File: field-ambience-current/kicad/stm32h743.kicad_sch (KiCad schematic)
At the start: 45 parts, among them J4 SWD 1.27mm (SWCLK/GND/SWDIO), U1 STM32H743VIT6 (480MHz M7, LQF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, Y1 8MHz ABLS-8.000MHZ-B4-T (CL=1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

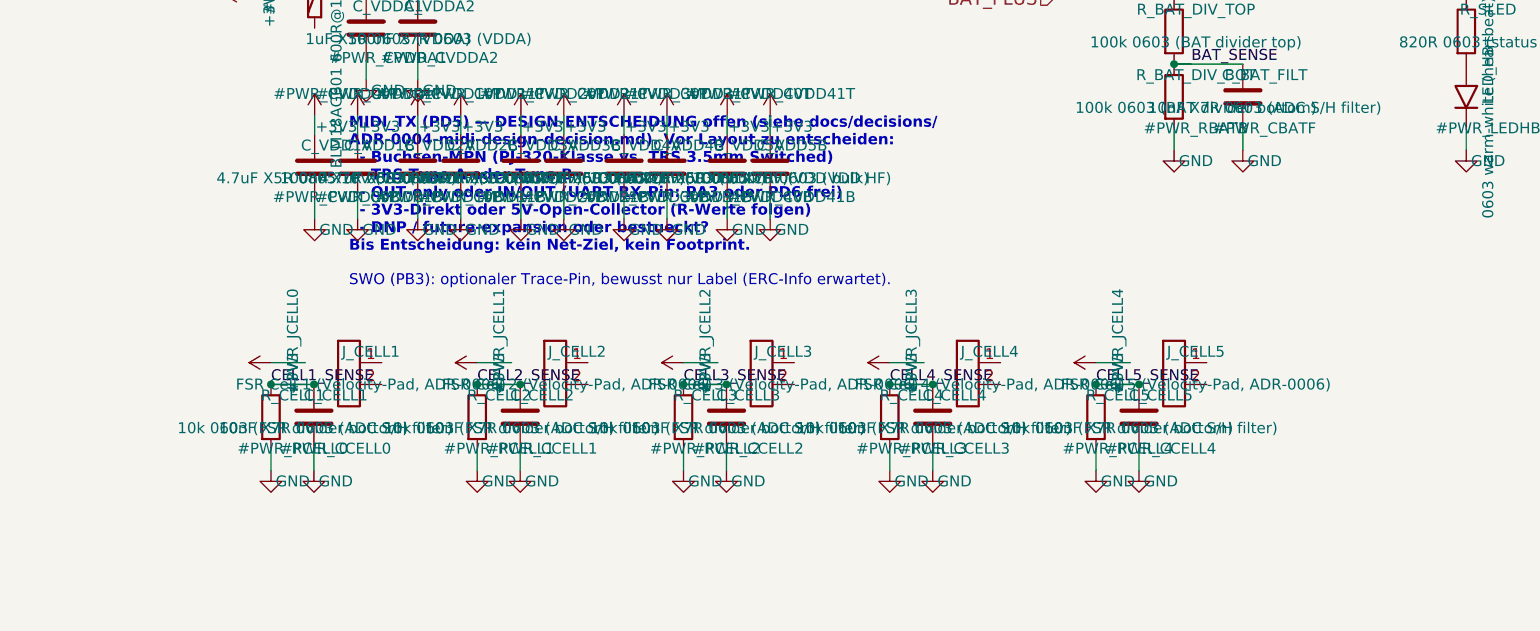
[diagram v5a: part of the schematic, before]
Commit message: pcb+fw(r18.14): Komponenten-Definition — 3D-Lib, 2 kritische BOM-Fixes, Encoder-Strategie (ADR-0012), Cell-Keys Magnetic-Hall (ADR-0013)
User-Direktive: Komponenten vor Layout definieren, 3D-Daten zu allem, Cells
wie HiChord mit langen Caps + Stabilizern, Encoder-Split + smooth + gleich
hoch + flach (Kick75), Encoder-UX-Bug fixen.

🔴 Kritische BOM-Fixes (via 3D-CAD-Abruf entdeckt):
- USB-C: C165935 war ein STF18N65M5-MOSFET (TO-220F-3)! Korrekt: C283540
  (TYPE-C-31-M-17, LCSC-verifiziert). Falsch seit r18.10.
- SW_BOOT: C720477 ist XUNPU TS-1088-AR02016 (nicht TS-1185A-C-A);
  FP von generisch TL3342 auf EasyEDA-verifiziertes SW_TS1088_SMD.

3D-STEP-Library:
- kicad/libraries/field_ambience.3dshapes/ — 9 Z-/Panel-kritische Modelle
- mechanical/3d_models/MANIFEST.md — Inventar, Höhen, Regenerier-Kommando

ADR-0012 Encoder-Strategie:
- EN3 (Display) einziger mit Push+Detents; EN1/2/4 = EC11E183440C smooth
  (ohne Rastung/Anschlag/Switch). Alle 4 = EC11E THT, gleiche Schaftlänge
  = gleich hoch, Ziel 20-22mm statt 24.5mm (EC11J-STEP-Beleg), Kick75-flach.
- EC11J SMD retired (NRND + zu hoch + Half-Step-Mismatch). FP-Verify: 0 offen.

Encoder-UX-Fix („zwei Klicks für 1%"):
- Bench-Encoder rastet jede halbe Quadratur-Periode → ENC_HALF_STEP Default=1
  (display_hw_test.c), Host-Test pinnt Full-Cycle-Modus explizit.
- encoders.c: per-Encoder substeps (Display 4, Smooth 2) + has_sw-Flag.
- 12/12 Test-Suiten PASS.

ADR-0013 Cell-Keys (ersetzt FSR aus ADR-0006):
- Gateron-LP-Magnetic-Switches (HiChord-Feel) + linearer Hall-Sensor pro
  Cell → Velocity = dPos/dt, Aftertouch firmware-offen. ADC-Pins unverändert.
- Lange Caps ≥2u mit LP-Stabilizern (Spacebar-Prinzip: Switch mittig,
  Support links/rechts).
- Schematic: J_CELL 1×2-FSR-Teiler → 1×3-Hall-Site + 1k-Serien-RC.
- Sensor-Kandidaten DRV5056A4/SS49E mit explizitem PINOUT-VERIFY (AP7361-Lektion).

Modifier-Buttons: SPEC stellt explizit klar — alle 5 identisch, momentary,
Latch-Zustand nur über LEDs (ADR-0008).

Scores: F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
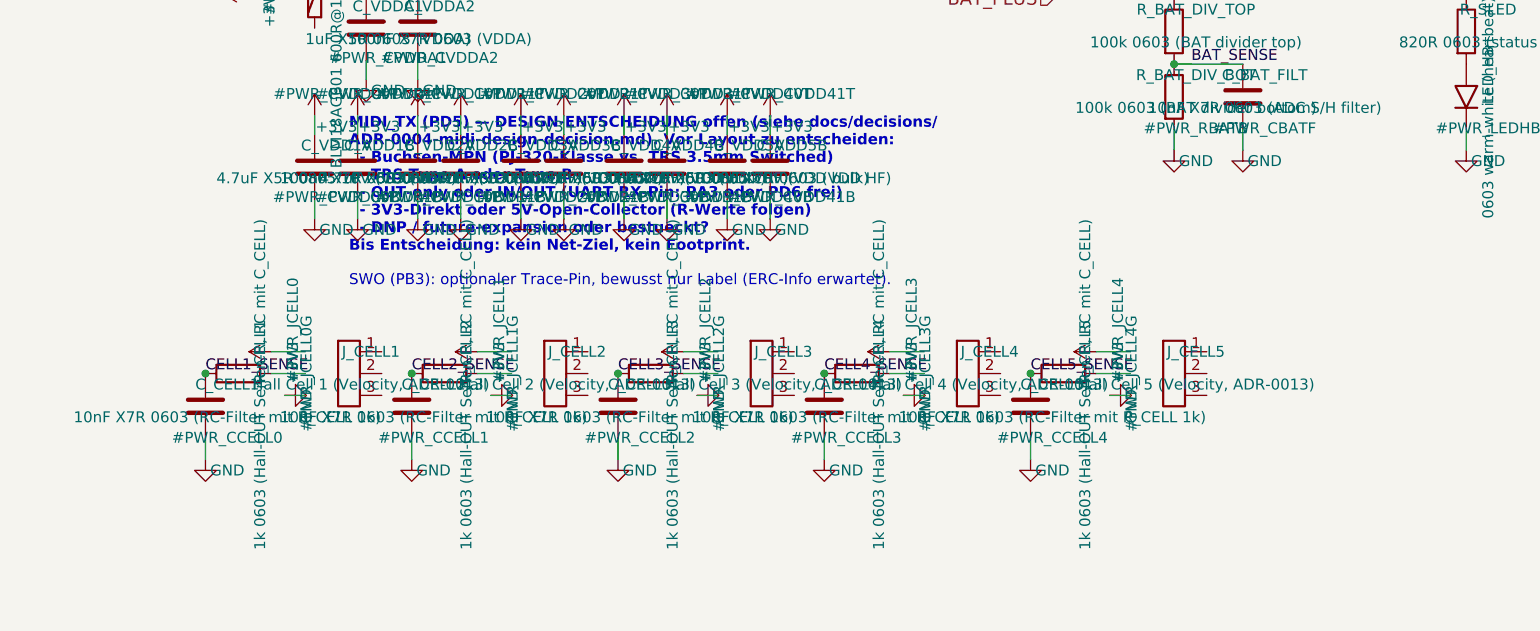
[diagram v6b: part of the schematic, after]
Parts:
- C_CELL1, C_CELL2, C_CELL3, C_CELL4, C_CELL5: value 10nF X7R 0603 (ADC S/H filter) -> 10nF X7R 0603 (RC-Filter mit R_CELL 1k)
- J_CELL1: value FSR Cell 1 (Velocity-Pad, ADR-0006) -> Hall Cell 1 (Velocity, ADR-0013); footprint Connector_PinHeader_2.54mm:PinHeader_1x02_P2.54mm_Vertical -> Connector_PinHeader_2.54mm:PinHeader_1x03_P2.54mm_Vertical; symbol Connector:Conn_01x02 -> Connector:Conn_01x03; FP_NOTE Anschluss-Art (Pin vs ZIF vs Laminat) folgt Mechanik-Design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 -> 1x3 2.54mm-Site: nimmt SS49E TO-92S direkt oder SOT-23-Brea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; LCSC TBD-VERIFY (FSR separat beschaffen, nicht JLC-bestueckt) -> TBD-VERIFY (DRV5056A4QDBZR auf LCSC pruefen; SS49E-Klone br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; MPN Interlink FSR 400 (Kandidat) -> DRV5056A4 (Kandidat) / SS49E-Klasse (Prototyp TO-92S); Mechanik (none) -> Sensor sitzt unter dem Magnet-Stem des Gateron-LP-Magnetic-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; PINOUT-VERIFY (none) -> Site-Reihenfolge 1=+3V3 2=OUT 3=GND ist SITE-Belegung, NICH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
- J_CELL2: value FSR Cell 2 (Velocity-Pad, ADR-0006) -> Hall Cell 2 (Velocity, ADR-0013); footprint Connector_PinHeader_2.54mm:PinHeader_1x02_P2.54mm_Vertical -> Connector_PinHeader_2.54mm:PinHeader_1x03_P2.54mm_Vertical; symbol Connector:Conn_01x02 -> Connector:Conn_01x03; FP_NOTE Anschluss-Art (Pin vs ZIF vs Laminat) folgt Mechanik-Design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 -> 1x3 2.54mm-Site: nimmt SS49E TO-92S direkt oder SOT-23-Brea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; LCSC TBD-VERIFY (FSR separat beschaffen, nicht JLC-bestueckt) -> TBD-VERIFY (DRV5056A4QDBZR auf LCSC pruefen; SS49E-Klone br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; MPN Interlink FSR 400 (Kandidat) -> DRV5056A4 (Kandidat) / SS49E-Klasse (Prototyp TO-92S); Mechanik (none) -> Sensor sitzt unter dem Magnet-Stem des Gateron-LP-Magnetic-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; PINOUT-VERIFY (none) -> Site-Reihenfolge 1=+3V3 2=OUT 3=GND ist SITE-Belegung, NICH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
- J_CELL3: value FSR Cell 3 (Velocity-Pad, ADR-0006) -> Hall Cell 3 (Velocity, ADR-0013); footprint Connector_PinHeader_2.54mm:PinHeader_1x02_P2.54mm_Vertical -> Connector_PinHeader_2.54mm:PinHeader_1x03_P2.54mm_Vertical; symbol Connector:Conn_01x02 -> Connector:Conn_01x03; FP_NOTE Anschluss-Art (Pin vs ZIF vs Laminat) folgt Mechanik-Design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 -> 1x3 2.54mm-Site: nimmt SS49E TO-92S direkt oder SOT-23-Brea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; LCSC TBD-VERIFY (FSR separat beschaffen, nicht JLC-bestueckt) -> TBD-VERIFY (DRV5056A4QDBZR auf LCSC pruefen; SS49E-Klone br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; MPN Interlink FSR 400 (Kandidat) -> DRV5056A4 (Kandidat) / SS49E-Klasse (Prototyp TO-92S); Mechanik (none) -> Sensor sitzt unter dem Magnet-Stem des Gateron-LP-Magnetic-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; PINOUT-VERIFY (none) -> Site-Reihenfolge 1=+3V3 2=OUT 3=GND ist SITE-Belegung, NICH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
- J_CELL4: value FSR Cell 4 (Velocity-Pad, ADR-0006) -> Hall Cell 4 (Velocity, ADR-0013); footprint Connector_PinHeader_2.54mm:PinHeader_1x02_P2.54mm_Vertical -> Connector_PinHeader_2.54mm:PinHeader_1x03_P2.54mm_Vertical; symbol Connector:Conn_01x02 -> Connector:Conn_01x03; FP_NOTE Anschluss-Art (Pin vs ZIF vs Laminat) folgt Mechanik-Design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 -> 1x3 2.54mm-Site: nimmt SS49E TO-92S direkt oder SOT-23-Brea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; LCSC TBD-VERIFY (FSR separat beschaffen, nicht JLC-bestueckt) -> TBD-VERIFY (DRV5056A4QDBZR auf LCSC pruefen; SS49E-Klone br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; MPN Interlink FSR 400 (Kandidat) -> DRV5056A4 (Kandidat) / SS49E-Klasse (Prototyp TO-92S); Mechanik (none) -> Sensor sitzt unter dem Magnet-Stem des Gateron-LP-Magnetic-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; PINOUT-VERIFY (none) -> Site-Reihenfolge 1=+3V3 2=OUT 3=GND ist SITE-Belegung, NICH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
- J_CELL5: value FSR Cell 5 (Velocity-Pad, ADR-0006) -> Hall Cell 5 (Velocity, ADR-0013); footprint Connector_PinHeader_2.54mm:PinHeader_1x02_P2.54mm_Vertical -> Connector_PinHeader_2.54mm:PinHeader_1x03_P2.54mm_Vertical; symbol Connector:Conn_01x02 -> Connector:Conn_01x03; FP_NOTE Anschluss-Art (Pin vs ZIF vs Laminat) folgt Mechanik-Design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 -> 1x3 2.54mm-Site: nimmt SS49E TO-92S direkt oder SOT-23-Brea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; LCSC TBD-VERIFY (FSR separat beschaffen, nicht JLC-bestueckt) -> TBD-VERIFY (DRV5056A4QDBZR auf LCSC pruefen; SS49E-Klone br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; MPN Interlink FSR 400 (Kandidat) -> DRV5056A4 (Kandidat) / SS49E-Klasse (Prototyp TO-92S); Mechanik (none) -> Sensor sitzt unter dem Magnet-Stem des Gateron-LP-Magnetic-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; PINOUT-VERIFY (none) -> Site-Reihenfolge 1=+3V3 2=OUT 3=GND ist SITE-Belegung, NICH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
- R_CELL1, R_CELL2, R_CELL3, R_CELL4, R_CELL5: value 10k 0603 (FSR divider bottom) -> 1k 0603 (Hall-OUT Serien-R, RC mit C_CELL); LCSC C25804 -> C21190; MPN 0603WAF1002T5E -> 0603WAF1001T5E
- SW_BOOT: footprint Button_Switch_SMD:SW_SPST_TL3342 -> field_ambience:SW_TS1088_SMD; FP_NOTE Mini-SMD-Tactile (kleinere Bauform als HX 12x12), nur fuer Service-Use bei Flash -> Mini-SMD-Tactile (kleinere Bauform als HX 12x12), nur fuer Service-Use bei Flash. r18.14: MPN korrigiert (war TS-1185A-C-A — C720477 ist XUNPU TS-1088-AR02016) + FP auf EasyEDA-verifiziertes Land-Pattern (3.9x2.9, P4.45) gewechselt; TL3342-FP passte nicht.; MPN TS-1185A-C-A -> TS-1088-AR02016
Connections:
- net GND: no longer R_CELL1.2, R_CELL2.2, R_CELL3.2, R_CELL4.2, R_CELL5.2
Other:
- moved on the sheet: C_CELL1, C_CELL2, C_CELL3, C_CELL4, C_CELL5, R_CELL1, R_CELL2, R_CELL3, R_CELL4, R_CELL5

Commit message: pcb(r18.14b): Komponenten-IDs verifiziert — EC11E + DRV5056
Drei verbleibende TBD-VERIFY-Punkte aus r18.14a geschlossen:

- EN3 Display: EC11E18244AU = C202365 (ALPS, 18P/36D + push, LCSC in stock)
- EN1/2/4 Smooth: EC11E183440C = C370986 (ALPS, 18P/no-detent + push,
  selbe Bauform → alle 4 gleich hoch verifiziert)
- Hall-Sensor: DRV5056A4QDBZR = C2152902 (TI SOT-23, 3.3V ratiometrisch)

DRV5056-Pinout aus TI-DS Table 4-1 verifiziert (statt geraten):
SOT-23: Pin 1=VCC, Pin 2=OUT, Pin 3=GND — matched 1:1 zur 1×3-Site.
TO-92-Variante (Prototyp) hat ABWEICHENDE Belegung (1=VCC/2=GND/3=OUT) —
Beine für Breadboard swappen.

Generator + SPEC §4 mit echten LCSC-IDs + Datasheet-URLs versorgt.
PROJECT_QUALITY BOM 8.5→9.

Offen für 10/10 BOM: Gateron-LP-Switches (Keyboard-Markt, kein LCSC),
470µF/16V Polymer 7343 (Web-Suche unzureichend, JLCPCB-GUI nötig),
220µF/10V MLCC 1210 (Samsung CL32A227MQVNNNE=C400951 ist 6.3V,
Headroom an 5V-PVDD knapp — 10V-Variante in Phase 6 final wählen).

https://claude.ai/code/session_01K5kLTFpDCCoYwx2dq6RkAv
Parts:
- J_CELL1, J_CELL2, J_CELL3, J_CELL4, J_CELL5: FP_NOTE 1x3 2.54mm-Site: nimmt SS49E TO-92S direkt oder SOT-23-Brea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 -> 1x3 2.54mm-Site fuer Prototyp. Phase 6: Site durch SOT-23-F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; LCSC TBD-VERIFY (DRV5056A4QDBZR auf LCSC pruefen; SS49E-Klone br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 -> C2152902; MPN DRV5056A4 (Kandidat) / SS49E-Klasse (Prototyp TO-92S) -> DRV5056A4QDBZR (TI, SOT-23, 3.3V ratiometrisch, unipolar, 0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; Manufacturer (none) -> Texas Instruments; PINOUT-VERIFIED (none) -> TI DRV5056 DS Table 4-1 (verifiziert r18.14): SOT-23 Pin 1=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; PINOUT-VERIFY Site-Reihenfolge 1=+3V3 2=OUT 3=GND ist SITE-Belegung, NICH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 -> (none)

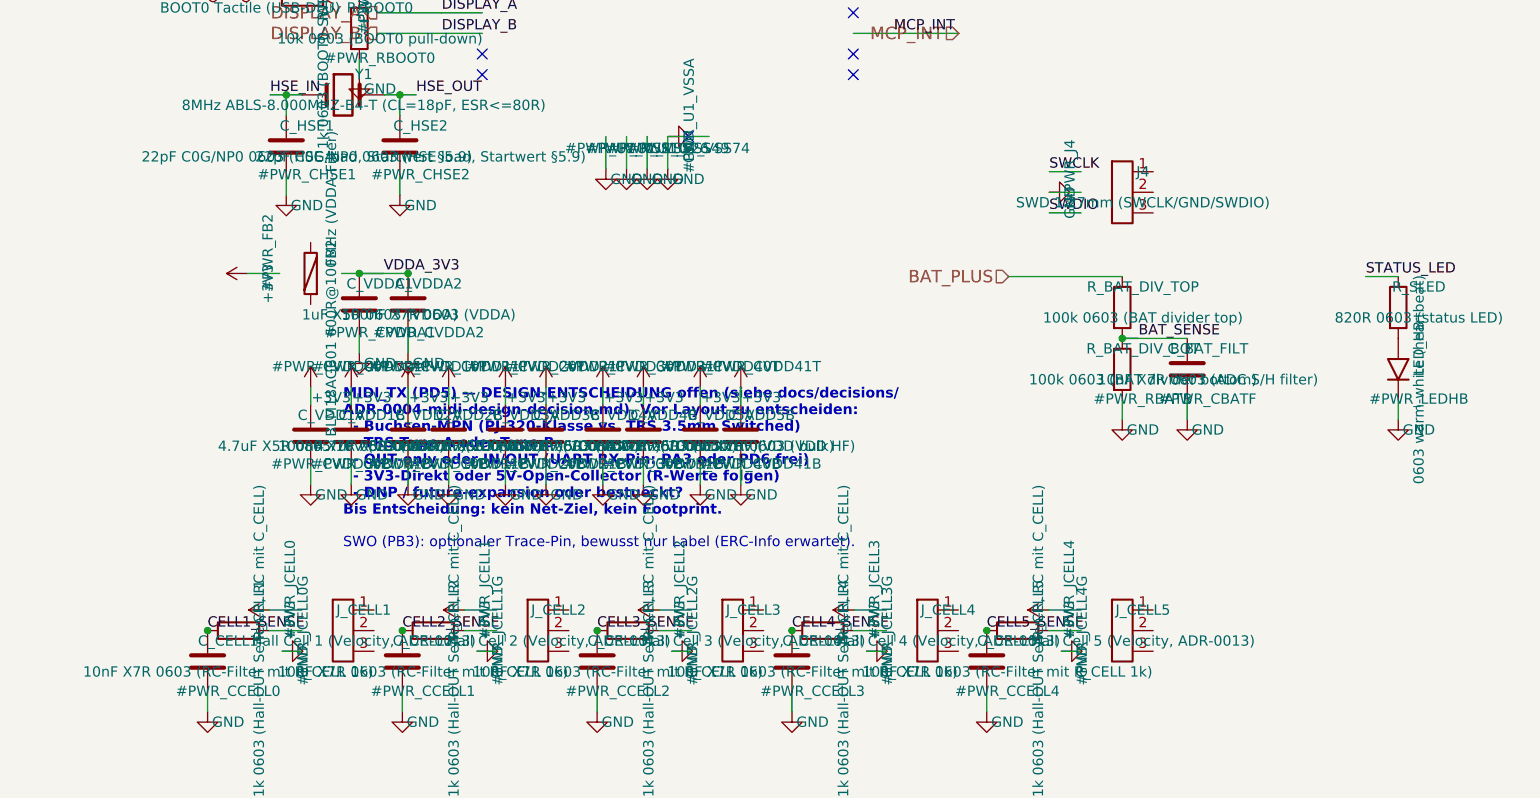
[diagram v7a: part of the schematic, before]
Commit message: pcb(r18.20): Audit-Folge-Fixes — Hall-SOT-23, HSE 27pF, SPEC-Frei-Liste, ADC-Channels
Autonome Schematic-Fixes aus dem Senior-Engineering-Audit:

🟠 HIGH — Hall-Sensor-Footprint auf echtes SOT-23
J_CELL1-5 hatten PinHeader_1x03-Platzhalter, verbaut wird DRV5056A4QDBZR
(SOT-23). PCB hätte 5 falsche Land-Patterns gehabt. → Package_TO_SOT_SMD:SOT-23.
Conn_01x03-Pin 1/2/3 → SOT-23-Pad 1/2/3 = VCC/OUT/GND (TI-DS Table 4-1).

🟠 HIGH — HSE-Load-Caps 22 → 27 pF
22pF implizierte C_stray=7pF (zu hoch). 27pF = 2*(CL 18 - C_stray 4.5).
Off-frequency-Start-Risiko (SAI-PLL3-Audio, USB-Sync) entschärft.

🟡 MEDIUM — SPEC §5.12 Frei-Liste: PC0/PC1/PA4/PB0/PB1 entfernt (seit r18.9
für CELL1..5_SENSE vergeben).

🟡 MEDIUM — ADC-Channel-Doku §5.6a: PC0=INP10, PC1=INP11, PA4=INP18,
PB0=INP9, PB1=INP5 — alle auf ADC1 (Scan-Mode reicht). Vor FW-ADC-Init
final gegen DS12110 Table 8 bestätigen.

Verifizierung: Generator regen, 8/8 paren-balanced, 5x SOT-23 (0 Header-
Leftovers), 27pF (0 22pF-Leftovers), CELL-Nets intakt, Firmware 13/13 PASS.

Offen → r18.20b (Sourcing-Agent läuft): C_HSE/C_BULK/MLCC-10V/LED-Farben LCSC.

https://claude.ai/code/session_01K5kLTFpDCCoYwx2dq6RkAv
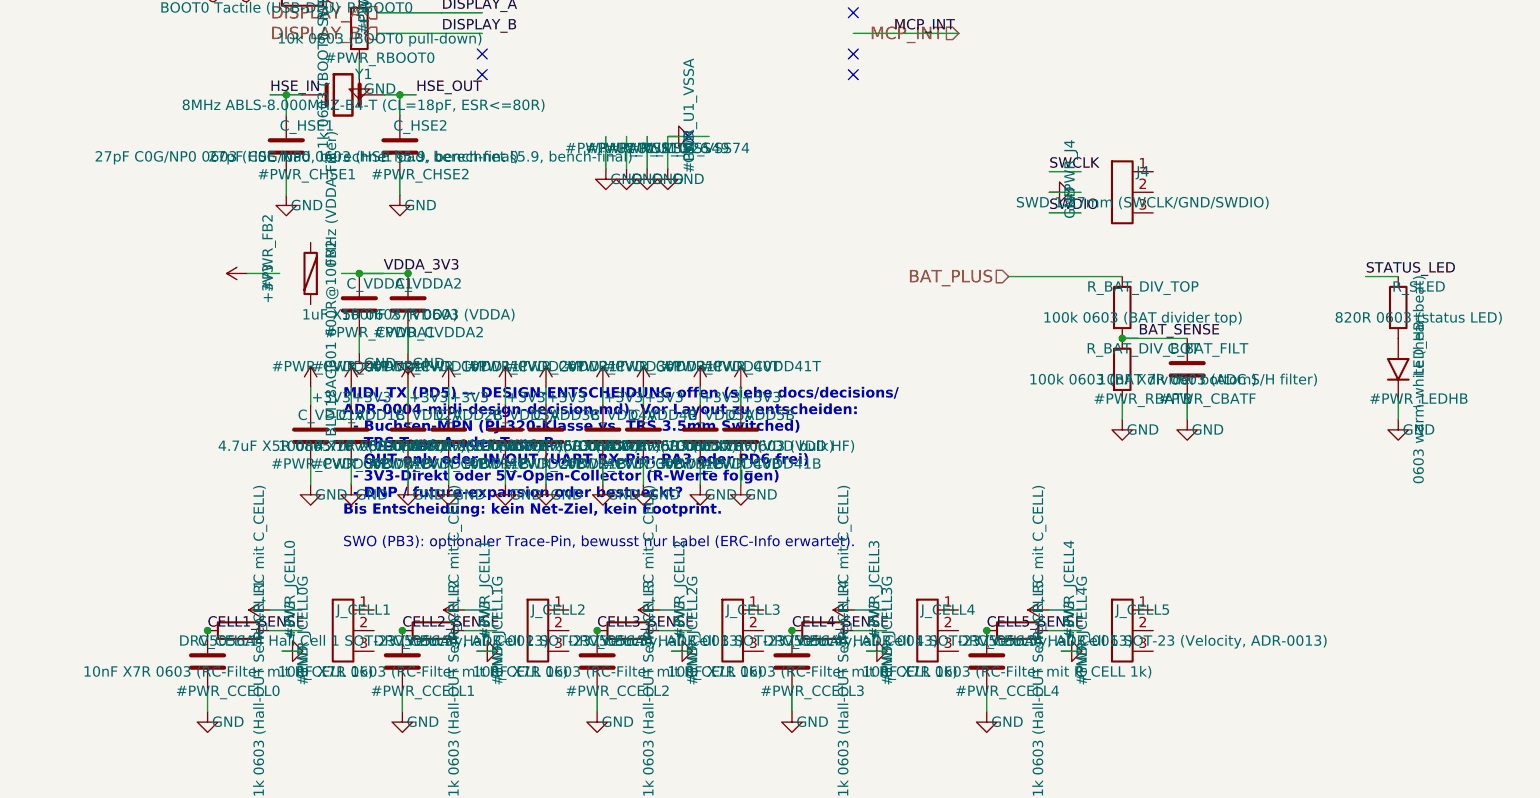
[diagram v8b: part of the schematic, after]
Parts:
- C_HSE1, C_HSE2: value 22pF C0G/NP0 0603 (HSE load, Startwert §5.9) -> 27pF C0G/NP0 0603 (HSE load, berechnet §5.9, bench-final); LCSC C1804 -> TBD-r18.20 (27pF C0G/NP0 50V 0603 — Sourcing-Agent); MPN CC0603JRNPO9BN220 -> CC0603JRNPO9BN270; VERIFY-STOCK 22pF +-5% C0G/NP0 50V 0603 -> 27pF +-5% C0G/NP0 50V 0603; vorher 22pF/C1804 (zu klein, C_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
- J_CELL1: value Hall Cell 1 (Velocity, ADR-0013) -> DRV5056A4 Hall Cell 1 SOT-23 (Velocity, ADR-0013); footprint Connector_PinHeader_2.54mm:PinHeader_1x03_P2.54mm_Vertical -> Package_TO_SOT_SMD:SOT-23; FP_NOTE 1x3 2.54mm-Site fuer Prototyp. Phase 6: Site durch SOT-23-F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 -> r18.20: SOT-23 final (Package_TO_SOT_SMD:SOT-23, KiCad-Stan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; PINOUT-VERIFIED TI DRV5056 DS Table 4-1 (verifiziert r18.14): SOT-23 Pin 1=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 -> TI DRV5056 DS Table 4-1 (r18.14): SOT-23 Pin 1=VCC, Pin 2=O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
- J_CELL2: value Hall Cell 2 (Velocity, ADR-0013) -> DRV5056A4 Hall Cell 2 SOT-23 (Velocity, ADR-0013); footprint Connector_PinHeader_2.54mm:PinHeader_1x03_P2.54mm_Vertical -> Package_TO_SOT_SMD:SOT-23; FP_NOTE 1x3 2.54mm-Site fuer Prototyp. Phase 6: Site durch SOT-23-F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 -> r18.20: SOT-23 final (Package_TO_SOT_SMD:SOT-23, KiCad-Stan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; PINOUT-VERIFIED TI DRV5056 DS Table 4-1 (verifiziert r18.14): SOT-23 Pin 1=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 -> TI DRV5056 DS Table 4-1 (r18.14): SOT-23 Pin 1=VCC, Pin 2=O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
- J_CELL3: value Hall Cell 3 (Velocity, ADR-0013) -> DRV5056A4 Hall Cell 3 SOT-23 (Velocity, ADR-0013); footprint Connector_PinHeader_2.54mm:PinHeader_1x03_P2.54mm_Vertical -> Package_TO_SOT_SMD:SOT-23; FP_NOTE 1x3 2.54mm-Site fuer Prototyp. Phase 6: Site durch SOT-23-F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 -> r18.20: SOT-23 final (Package_TO_SOT_SMD:SOT-23, KiCad-Stan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; PINOUT-VERIFIED TI DRV5056 DS Table 4-1 (verifiziert r18.14): SOT-23 Pin 1=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 -> TI DRV5056 DS Table 4-1 (r18.14): SOT-23 Pin 1=VCC, Pin 2=O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
- J_CELL4: value Hall Cell 4 (Velocity, ADR-0013) -> DRV5056A4 Hall Cell 4 SOT-23 (Velocity, ADR-0013); footprint Connector_PinHeader_2.54mm:PinHeader_1x03_P2.54mm_Vertical -> Package_TO_SOT_SMD:SOT-23; FP_NOTE 1x3 2.54mm-Site fuer Prototyp. Phase 6: Site durch SOT-23-F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 -> r18.20: SOT-23 final (Package_TO_SOT_SMD:SOT-23, KiCad-Stan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; PINOUT-VERIFIED TI DRV5056 DS Table 4-1 (verifiziert r18.14): SOT-23 Pin 1=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 -> TI DRV5056 DS Table 4-1 (r18.14): SOT-23 Pin 1=VCC, Pin 2=O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
- J_CELL5: value Hall Cell 5 (Velocity, ADR-0013) -> DRV5056A4 Hall Cell 5 SOT-23 (Velocity, ADR-0013); footprint Connector_PinHeader_2.54mm:PinHeader_1x03_P2.54mm_Vertical -> Package_TO_SOT_SMD:SOT-23; FP_NOTE 1x3 2.54mm-Site fuer Prototyp. Phase 6: Site durch SOT-23-F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 -> r18.20: SOT-23 final (Package_TO_SOT_SMD:SOT-23, KiCad-Stan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; PINOUT-VERIFIED TI DRV5056 DS Table 4-1 (verifiziert r18.14): SOT-23 Pin 1=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 -> TI DRV5056 DS Table 4-1 (r18.14): SOT-23 Pin 1=VCC, Pin 2=O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
